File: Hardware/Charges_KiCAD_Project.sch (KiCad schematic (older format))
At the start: 33 parts, among them IC1 TP124005-2, J1 TB002-500-04BE, J2 TB002-500-04BE, Q1 SI7232DN-T1-GE3, Q2 SI7232DN-T1-GE3

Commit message: Changes to PCB size and components
PCB size was changed by adding 3mm to the top and bottom, the screw terminal was switched to a 90 degree angle one, and the libraries were updated
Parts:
- J1, J2: value TB002-500-04BE -> 796684-4; footprint SamacSys_Parts:TB00250004BE -> RDT_Custom_Footprints:TB00250004BE
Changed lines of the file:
@@
 P 7400 5500
 F 0 "J1" H 8028 5396 50  0000 L CNN
-F 1 "TB002-500-04BE" H 8028 5305 50  0000 L CNN
-F 2 "SamacSys_Parts:TB00250004BE" H 8050 5600 50  0001 L CNN
+F 1 "796684-4" H 8028 5305 50  0000 L CNN
+F 2 "RDT_Custom_Footprints:TB00250004BE" H 8050 5600 50  0001 L CNN
 F 3 "https://componentsearchengine.com/Datasheets/1/TB002-500-04BE.pdf" H 8050 5500 50  0001 L CNN
 F 4 "Fixed Terminal Blocks screw type, 5.00 , horizontal, 4 poles, CUI Blue, slotted screw, PCB mount" H 8050 5400 50  0001 L CNN "Description"
@@
 P 9850 5500
 F 0 "J2" H 10478 5396 50  0000 L CNN
-F 1 "TB002-500-04BE" H 10478 5305 50  0000 L CNN
-F 2 "SamacSys_Parts:TB00250004BE" H 10500 5600 50  0001 L CNN
+F 1 "796684-4" H 10478 5305 50  0000 L CNN
+F 2 "RDT_Custom_Footprints:TB00250004BE" H 10500 5600 50  0001 L CNN
 F 3 "https://componentsearchengine.com/Datasheets/1/TB002-500-04BE.pdf" H 10500 5500 50  0001 L CNN
 F 4 "Fixed Terminal Blocks screw type, 5.00 , horizontal, 4 poles, CUI Blue, slotted screw, PCB mount" H 10500 5400 50  0001 L CNN "Description"

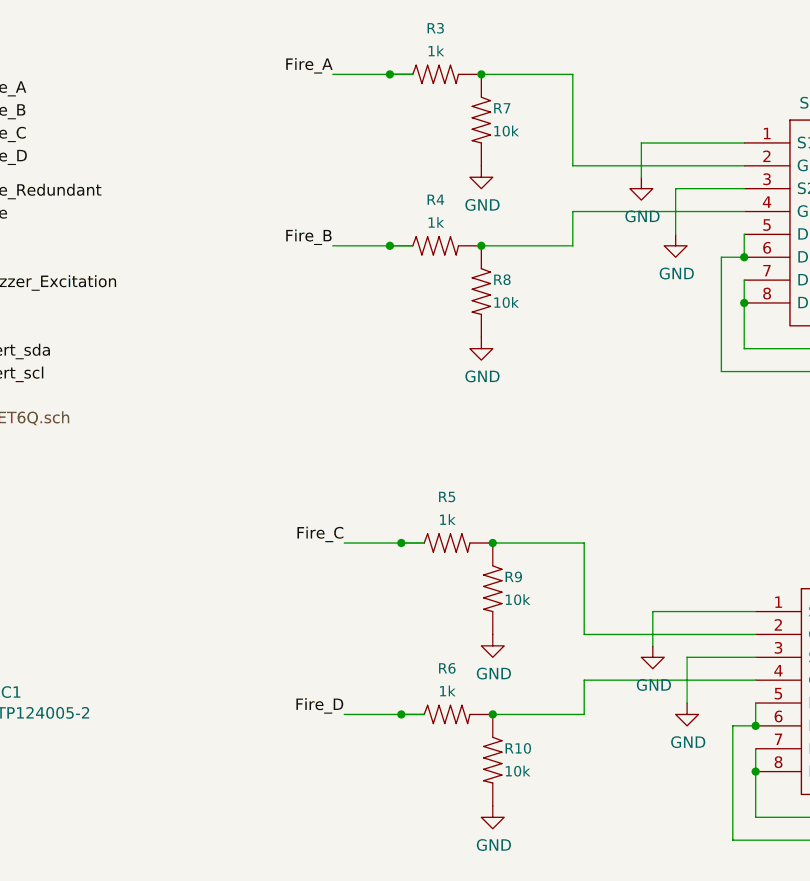
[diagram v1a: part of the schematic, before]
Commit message: Replaced passive component footprints with handsolder variants
Most components unaffected, redesign was needed around SI7232DN chips
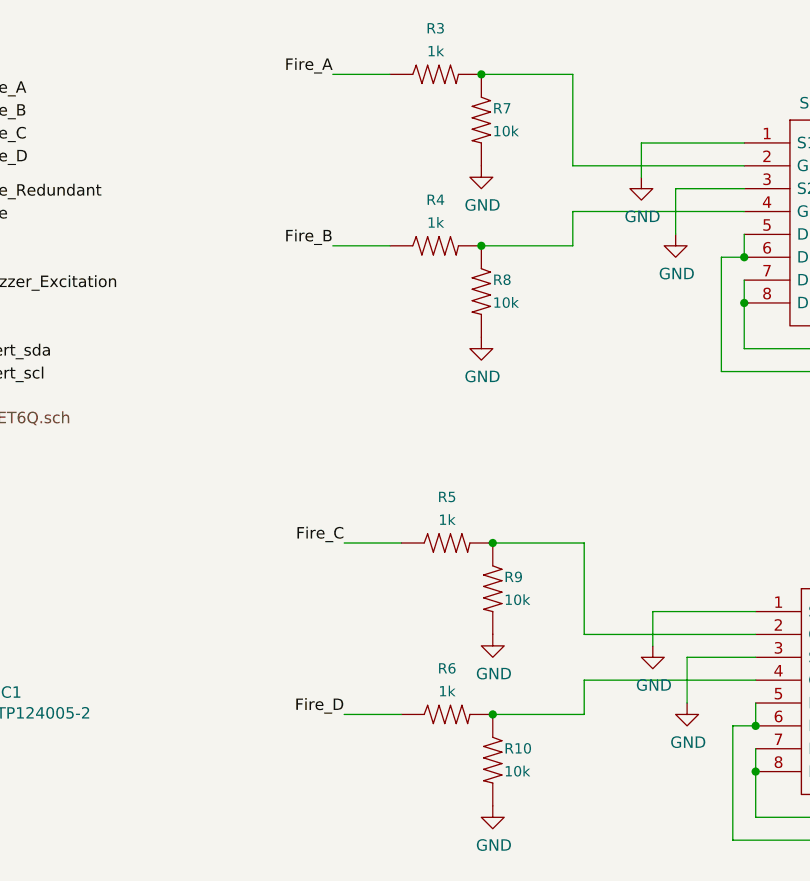
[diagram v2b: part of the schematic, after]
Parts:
- R1, R10, R11, R12, R13, R14, R15, R16, R17, R18, R19, R2, R20, R21, R22, R23, R24, R3, R4, R5, R6, R7, R8, R9: footprint Resistor_SMD:R_0603_1608Metric -> Resistor_SMD:R_0603_1608Metric_Pad1.05x0.95mm_HandSolder
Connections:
- wire segments 113 -> 109
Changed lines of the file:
@@
 Wire Wire Line
 	6650 3000 6400 3000
-Connection ~ 6650 3000
 Connection ~ 7050 3750
 Wire Wire Line
 	6650 3750 6400 3750
-Connection ~ 6650 3750
 $Comp
 L Charges_KiCAD_Project-rescue:RESISTOR0402-SparkFun-Resistors R9
@@
 F 0 "R9" V 7000 3250 45  0000 L CNN
 F 1 "10k" V 7100 3250 45  0000 L CNN
-F 2 "Resistor_SMD:R_0603_1608Metric" H 7050 3350 20  0001 C CNN
+F 2 "Resistor_SMD:R_0603_1608Metric_Pad1.05x0.95mm_HandSolder" H 7050 3350 20  0001 C CNN
 F 3 "" H 7050 3200 60  0001 C CNN
 F 4 " " V 7134 3268 60  0000 L CNN "Field4"
@@
 	1    0    0    -1
 $EndComp
-Wire Wire Line
-	6750 3000 6650 3000
 $Comp
 L power:GND #PWR010
@@
 F 0 "R10" V 7000 4000 45  0000 L CNN
 F 1 "10k" V 7100 4000 45  0000 L CNN
-F 2 "Resistor_SMD:R_0603_1608Metric" H 7050 4100 20  0001 C CNN
+F 2 "Resistor_SMD:R_0603_1608Metric_Pad1.05x0.95mm_HandSolder" H 7050 4100 20  0001 C CNN
 F 3 "" H 7050 3950 60  0001 C CNN
 F 4 " " V 7134 4018 60  0000 L CNN "Field4"
@@
 F 0 "R6" H 6850 3950 45  0000 C CNN
 F 1 "1k" H 6850 3850 45  0000 C CNN
-F 2 "Resistor_SMD:R_0603_1608Metric" H 6850 3900 20  0001 C CNN
+F 2 "Resistor_SMD:R_0603_1608Metric_Pad1.05x0.95mm_HandSolder" H 6850 3900 20  0001 C CNN
 F 3 "" H 6850 3750 60  0001 C CNN
 F 4 " " H 6850 3871 60  0000 C CNN "Field4"
@@
 	1    0    0    -1
 $EndComp
-Wire Wire Line
-	6750 3750 6650 3750
 Wire Wire Line
 	10450 3950 10700 3950
@@
 F 0 "R23" V 10400 3400 45  0000 L CNN
 F 1 "27k" V 10500 3400 45  0000 L CNN
-F 2 "Resistor_SMD:R_0603_1608Metric" H 10450 3450 20  0001 C CNN
+F 2 "Resistor_SMD:R_0603_1608Metric_Pad1.05x0.95mm_HandSolder" H 10450 3450 20  0001 C CNN
 F 3 "" H 10450 3300 60  0001 C CNN
 F 4 " " V 10534 3368 60  0000 L CNN "Field4"
@@
 F 0 "R19" H 10250 3250 45  0000 C CNN
 F 1 "100k" H 10250 3200 45  0000 C CNN
-F 2 "Resistor_SMD:R_0603_1608Metric" H 10250 3250 20  0001 C CNN
+F 2 "Resistor_SMD:R_0603_1608Metric_Pad1.05x0.95mm_HandSolder" H 10250 3250 20  0001 C CNN
 F 3 "" H 10250 3100 60  0001 C CNN
 F 4 " " H 10250 3221 60  0000 C CNN "Field4"
@@
 F 0 "R24" V 10400 4250 45  0000 L CNN
 F 1 "27k" V 10500 4250 45  0000 L CNN
-F 2 "Resistor_SMD:R_0603_1608Metric" H 10450 4300 20  0001 C CNN
+F 2 "Resistor_SMD:R_0603_1608Metric_Pad1.05x0.95mm_HandSolder" H 10450 4300 20  0001 C CNN
 F 3 "" H 10450 4150 60  0001 C CNN
 F 4 " " V 10534 4218 60  0000 L CNN "Field4"
@@
 F 0 "R20" H 10250 4100 45  0000 C CNN
 F 1 "100k" H 10250 4050 45  0000 C CNN
-F 2 "Resistor_SMD:R_0603_1608Metric" H 10250 4100 20  0001 C CNN
+F 2 "Resistor_SMD:R_0603_1608Metric_Pad1.05x0.95mm_HandSolder" H 10250 4100 20  0001 C CNN
 F 3 "" H 10250 3950 60  0001 C CNN
 F 4 " " H 10250 4071 60  0000 C CNN "Field4"
@@
 F 0 "R5" H 6850 3200 45  0000 C CNN
 F 1 "1k" H 6850 3100 45  0000 C CNN
-F 2 "Resistor_SMD:R_0603_1608Metric" H 6850 3150 20  0001 C CNN
+F 2 "Resistor_SMD:R_0603_1608Metric_Pad1.05x0.95mm_HandSolder" H 6850 3150 20  0001 C CNN
 F 3 "" H 6850 3000 60  0001 C CNN
 F 4 " " H 6850 3121 60  0000 C CNN "Field4"
@@
 Wire Wire Line
 	6600 950  6350 950
-Connection ~ 6600 950
 Connection ~ 7000 1700
 Wire Wire Line
 	6600 1700 6350 1700
-Connection ~ 6600 1700
 $Comp
 L Charges_KiCAD_Project-rescue:RESISTOR0402-SparkFun-Resistors R7
@@
 F 0 "R7" V 6950 1200 45  0000 L CNN
 F 1 "10k" V 7050 1200 45  0000 L CNN
-F 2 "Resistor_SMD:R_0603_1608Metric" H 7000 1300 20  0001 C CNN
+F 2 "Resistor_SMD:R_0603_1608Metric_Pad1.05x0.95mm_HandSolder" H 7000 1300 20  0001 C CNN
 F 3 "" H 7000 1150 60  0001 C CNN
 F 4 " " V 7084 1218 60  0000 L CNN "Field4"
@@
 	1    0    0    -1
 $EndComp
-Wire Wire Line
-	6700 950  6600 950
 $Comp
 L power:GND #PWR08
@@
 F 0 "R8" V 6950 1950 45  0000 L CNN
 F 1 "10k" V 7050 1950 45  0000 L CNN
-F 2 "Resistor_SMD:R_0603_1608Metric" H 7000 2050 20  0001 C CNN
+F 2 "Resistor_SMD:R_0603_1608Metric_Pad1.05x0.95mm_HandSolder" H 7000 2050 20  0001 C CNN
 F 3 "" H 7000 1900 60  0001 C CNN
 F 4 " " V 7084 1968 60  0000 L CNN "Field4"
@@
 F 0 "R15" H 9500 5650 45  0000 C CNN
 F 1 "0.25" H 9500 5600 45  0000 C CNN
-F 2 "Resistor_SMD:R_0603_1608Metric" H 9500 5650 20  0001 C CNN
+F 2 "Resistor_SMD:R_0603_1608Metric_Pad1.05x0.95mm_HandSolder" H 9500 5650 20  0001 C CNN
 F 3 "" H 9500 5500 60  0001 C CNN
 F 4 " " H 9500 5621 60  0000 C CNN "Field4"
@@
 F 0 "R13" H 9100 5400 45  0000 C CNN
 F 1 "10" H 9100 5350 45  0000 C CNN
-F 2 "Resistor_SMD:R_0603_1608Metric" H 9100 5650 20  0001 C CNN
+F 2 "Resistor_SMD:R_0603_1608Metric_Pad1.05x0.95mm_HandSolder" H 9100 5650 20  0001 C CNN
 F 3 "" H 9100 5500 60  0001 C CNN
 F 4 " " H 9100 5621 60  0000 C CNN "Field4"
@@
 F 0 "R14" H 9100 5700 45  0000 C CNN
 F 1 "10" H 9100 5650 45  0000 C CNN
-F 2 "Resistor_SMD:R_0603_1608Metric" H 9100 5950 20  0001 C CNN
+F 2 "Resistor_SMD:R_0603_1608Metric_Pad1.05x0.95mm_HandSolder" H 9100 5950 20  0001 C CNN
 F 3 "" H 9100 5800 60  0001 C CNN
 F 4 " " H 9100 5921 60  0000 C CNN "Field4"
@@
 F 0 "R16" H 9500 5950 45  0000 C CNN
 F 1 "0.25" H 9500 5900 45  0000 C CNN
-F 2 "Resistor_SMD:R_0603_1608Metric" H 9500 5950 20  0001 C CNN
+F 2 "Resistor_SMD:R_0603_1608Metric_Pad1.05x0.95mm_HandSolder" H 9500 5950 20  0001 C CNN
 F 3 "" H 9500 5800 60  0001 C CNN
 F 4 " " H 9500 5921 60  0000 C CNN "Field4"
@@
 F 0 "R4" H 6800 1900 45  0000 C CNN
 F 1 "1k" H 6800 1800 45  0000 C CNN
-F 2 "Resistor_SMD:R_0603_1608Metric" H 6800 1850 20  0001 C CNN
+F 2 "Resistor_SMD:R_0603_1608Metric_Pad1.05x0.95mm_HandSolder" H 6800 1850 20  0001 C CNN
 F 3 "" H 6800 1700 60  0001 C CNN
 F 4 " " H 6800 1821 60  0000 C CNN "Field4"
@@
 F 0 "R21" V 10350 1350 45  0000 L CNN
 F 1 "27k" V 10450 1350 45  0000 L CNN
-F 2 "Resistor_SMD:R_0603_1608Metric" H 10400 1400 20  0001 C CNN
+F 2 "Resistor_SMD:R_0603_1608Metric_Pad1.05x0.95mm_HandSolder" H 10400 1400 20  0001 C CNN
 F 3 "" H 10400 1250 60  0001 C CNN
 F 4 " " V 10484 1318 60  0000 L CNN "Field4"
@@
 F 0 "R17" H 10200 1200 45  0000 C CNN
 F 1 "100k" H 10200 1150 45  0000 C CNN
-F 2 "Resistor_SMD:R_0603_1608Metric" H 10200 1200 20  0001 C CNN
+F 2 "Resistor_SMD:R_0603_1608Metric_Pad1.05x0.95mm_HandSolder" H 10200 1200 20  0001 C CNN
 F 3 "" H 10200 1050 60  0001 C CNN
 F 4 " " H 10200 1171 60  0000 C CNN "Field4"
@@
 F 0 "R22" V 10350 2200 45  0000 L CNN
 F 1 "27k" V 10450 2200 45  0000 L CNN
-F 2 "Resistor_SMD:R_0603_1608Metric" H 10400 2250 20  0001 C CNN
+F 2 "Resistor_SMD:R_0603_1608Metric_Pad1.05x0.95mm_HandSolder" H 10400 2250 20  0001 C CNN
 F 3 "" H 10400 2100 60  0001 C CNN
 F 4 " " V 10484 2168 60  0000 L CNN "Field4"
@@
 F 0 "R3" H 6800 1150 45  0000 C CNN
 F 1 "1k" H 6800 1050 45  0000 C CNN
-F 2 "Resistor_SMD:R_0603_1608Metric" H 6800 1100 20  0001 C CNN
+F 2 "Resistor_SMD:R_0603_1608Metric_Pad1.05x0.95mm_HandSolder" H 6800 1100 20  0001 C CNN
 F 3 "" H 6800 950 60  0001 C CNN
 F 4 " " H 6800 1071 60  0000 C CNN "Field4"
@@
 F 0 "R18" H 10200 2050 45  0000 C CNN
 F 1 "100k" H 10200 2000 45  0000 C CNN
-F 2 "Resistor_SMD:R_0603_1608Metric" H 10200 2050 20  0001 C CNN
+F 2 "Resistor_SMD:R_0603_1608Metric_Pad1.05x0.95mm_HandSolder" H 10200 2050 20  0001 C CNN
 F 3 "" H 10200 1900 60  0001 C CNN
 F 4 " " H 10200 2021 60  0000 C CNN "Field4"
@@
 	1    0    0    -1
 $EndComp
-Wire Wire Line
-	6700 1700 6600 1700
 $Comp
 L Charges_KiCAD_Project-rescue:SI7232DN-T1-GE3-SamacSys_Parts Q1
@@
 F 0 "R2" H 6650 5700 45  0000 C CNN
 F 1 "10" H 6650 5650 45  0000 C CNN
-F 2 "Resistor_SMD:R_0603_1608Metric" H 6650 5950 20  0001 C CNN
+F 2 "Resistor_SMD:R_0603_1608Metric_Pad1.05x0.95mm_HandSolder" H 6650 5950 20  0001 C CNN
 F 3 "" H 6650 5800 60  0001 C CNN
 F 4 " " H 6650 5921 60  0000 C CNN "Field4"
@@
 F 0 "R1" H 6650 5400 45  0000 C CNN
 F 1 "10" H 6650 5350 45  0000 C CNN
-F 2 "Resistor_SMD:R_0603_1608Metric" H 6650 5650 20  0001 C CNN
+F 2 "Resistor_SMD:R_0603_1608Metric_Pad1.05x0.95mm_HandSolder" H 6650 5650 20  0001 C CNN
 F 3 "" H 6650 5500 60  0001 C CNN
 F 4 " " H 6650 5621 60  0000 C CNN "Field4"
@@
 F 0 "R12" H 7050 5950 45  0000 C CNN
 F 1 "0.25" H 7050 5900 45  0000 C CNN
-F 2 "Resistor_SMD:R_0603_1608Metric" H 7050 5950 20  0001 C CNN
+F 2 "Resistor_SMD:R_0603_1608Metric_Pad1.05x0.95mm_HandSolder" H 7050 5950 20  0001 C CNN
 F 3 "" H 7050 5800 60  0001 C CNN
 F 4 " " H 7050 5921 60  0000 C CNN "Field4"
@@
 F 0 "R11" H 7050 5650 45  0000 C CNN
 F 1 "0.25" H 7050 5600 45  0000 C CNN
-F 2 "Resistor_SMD:R_0603_1608Metric" H 7050 5650 20  0001 C CNN
+F 2 "Resistor_SMD:R_0603_1608Metric_Pad1.05x0.95mm_HandSolder" H 7050 5650 20  0001 C CNN
 F 3 "" H 7050 5500 60  0001 C CNN
 F 4 " " H 7050 5621 60  0000 C CNN "Field4"

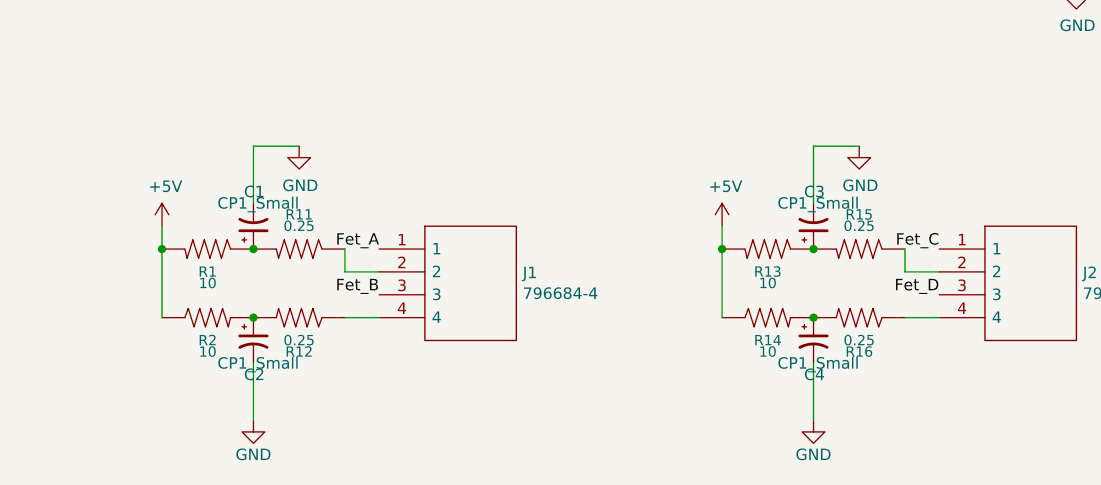
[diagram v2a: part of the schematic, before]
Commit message: update to caps and board layout
caps were changed and resistors were removed as they were not needed
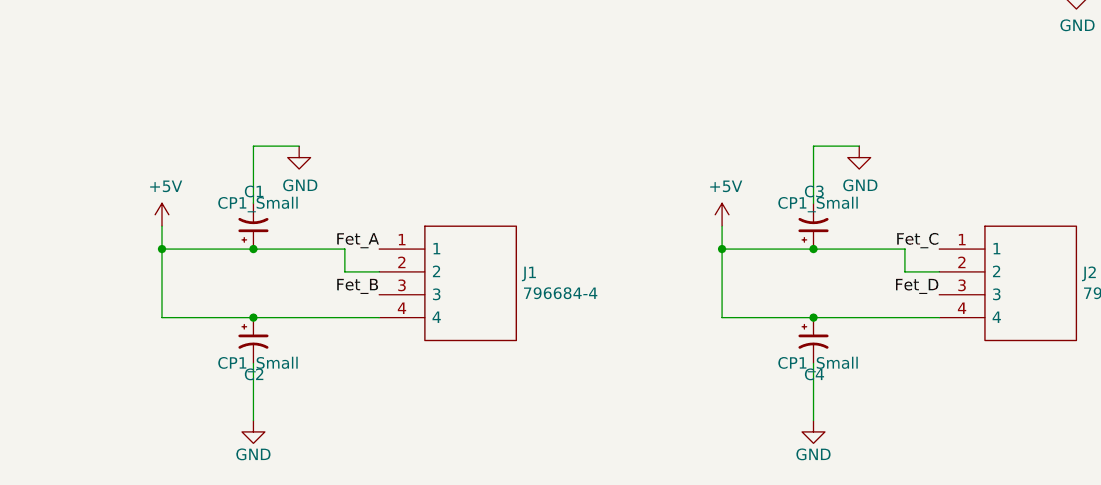
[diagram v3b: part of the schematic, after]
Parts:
- removed R1, R13, R14, R2: 10, Resistor_SMD:R_0603_1608Metric_Pad1.05x0.95mm_HandSolder, symbol Charges_KiCAD_Project-rescue:RESISTOR0402-SparkFun-Resistors
- removed R11, R12, R15, R16: 0.25, Resistor_SMD:R_0603_1608Metric_Pad1.05x0.95mm_HandSolder, symbol Charges_KiCAD_Project-rescue:RESISTOR0402-SparkFun-Resistors
- C1, C2, C3, C4: footprint Capacitor_THT:CP_Axial_L10.0mm_D4.5mm_P15.00mm_Horizontal -> Capacitor_THT:CP_Axial_L18.0mm_D6.5mm_P25.00mm_Horizontal
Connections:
- net +5V: now also C1.1, C2.1, C3.1, C4.1, J1.2, J1.4, J2.2, J2.4
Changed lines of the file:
@@
 	1    0    0    -1
 $EndComp
-Wire Wire Line
-	8900 5500 8900 5400
-Connection ~ 8900 5500
 $Comp
 L power:GND #PWR02
@@
 $EndComp
 Wire Wire Line
-	7400 5800 7250 5800
-Wire Wire Line
 	7250 5600 7400 5600
 Text Label 7400 5500 2    50   ~ 0
@@
 F 0 "C2" H 6900 5750 50  0000 R CNN
 F 1 "CP1_Small" H 7050 5800 50  0000 R CNN
-F 2 "Capacitor_THT:CP_Axial_L10.0mm_D4.5mm_P15.00mm_Horizontal" H 6850 5900 50  0001 C CNN
+F 2 "Capacitor_THT:CP_Axial_L18.0mm_D6.5mm_P25.00mm_Horizontal" H 6850 5900 50  0001 C CNN
 F 3 "~" H 6850 5900 50  0001 C CNN
 	1    6850 5900
 	1    0    0    -1
 $EndComp
-Connection ~ 6850 5800
 Wire Wire Line
 	6850 6000 6850 6250
@@
 	1    0    0    -1
 $EndComp
-Connection ~ 6850 5500
 $Comp
 L Device:CP1_Small C1
@@
 F 0 "C1" H 6900 5250 50  0000 R CNN
 F 1 "CP1_Small" H 7050 5300 50  0000 R CNN
-F 2 "Capacitor_THT:CP_Axial_L10.0mm_D4.5mm_P15.00mm_Horizontal" H 6850 5400 50  0001 C CNN
+F 2 "Capacitor_THT:CP_Axial_L18.0mm_D6.5mm_P25.00mm_Horizontal" H 6850 5400 50  0001 C CNN
 F 3 "~" H 6850 5400 50  0001 C CNN
 	1    6850 5400
@@
 Wire Wire Line
 	7250 5600 7250 5500
-Wire Wire Line
-	6450 5800 6450 5500
-Wire Wire Line
-	6450 5500 6450 5400
-Connection ~ 6450 5500
 $Comp
 L power:+5V #PWR05
@@
 Wire Wire Line
 	1050 3800 1150 3800
-Wire Wire Line
-	8900 5800 8900 5500
 Text Label 2350 2150 0    50   ~ 0
 Fire_Redundant
@@
 F 0 "C3" H 9350 5250 50  0000 R CNN
 F 1 "CP1_Small" H 9500 5300 50  0000 R CNN
-F 2 "Capacitor_THT:CP_Axial_L10.0mm_D4.5mm_P15.00mm_Horizontal" H 9300 5400 50  0001 C CNN
+F 2 "Capacitor_THT:CP_Axial_L18.0mm_D6.5mm_P25.00mm_Horizontal" H 9300 5400 50  0001 C CNN
 F 3 "~" H 9300 5400 50  0001 C CNN
 	1    9300 5400
 	1    0    0    1
 $EndComp
-$Comp
-L Charges_KiCAD_Project-rescue:RESISTOR0402-SparkFun-Resistors R15
-U 1 1 61951EFA
-P 9500 5500
-F 0 "R15" H 9500 5650 45  0000 C CNN
-F 1 "0.25" H 9500 5600 45  0000 C CNN
-F 2 "Resistor_SMD:R_0603_1608Metric_Pad1.05x0.95mm_HandSolder" H 9500 5650 20  0001 C CNN
-F 3 "" H 9500 5500 60  0001 C CNN
-F 4 " " H 9500 5621 60  0000 C CNN "Field4"
-	1    9500 5500
-	-1   0    0    -1
-$EndComp
-$Comp
-L Charges_KiCAD_Project-rescue:RESISTOR0402-SparkFun-Resistors R13
-U 1 1 61951EF3
-P 9100 5500
-F 0 "R13" H 9100 5400 45  0000 C CNN
-F 1 "10" H 9100 5350 45  0000 C CNN
-F 2 "Resistor_SMD:R_0603_1608Metric_Pad1.05x0.95mm_HandSolder" H 9100 5650 20  0001 C CNN
-F 3 "" H 9100 5500 60  0001 C CNN
-F 4 " " H 9100 5621 60  0000 C CNN "Field4"
-	1    9100 5500
-	-1   0    0    -1
-$EndComp
-Connection ~ 9300 5500
 $Comp
 L power:GND #PWR018
@@
 Wire Wire Line
 	9300 6000 9300 6250
-Connection ~ 9300 5800
-$Comp
-L Charges_KiCAD_Project-rescue:RESISTOR0402-SparkFun-Resistors R14
-U 1 1 61951EDB
-P 9100 5800
-F 0 "R14" H 9100 5700 45  0000 C CNN
-F 1 "10" H 9100 5650 45  0000 C CNN
-F 2 "Resistor_SMD:R_0603_1608Metric_Pad1.05x0.95mm_HandSolder" H 9100 5950 20  0001 C CNN
-F 3 "" H 9100 5800 60  0001 C CNN
-F 4 " " H 9100 5921 60  0000 C CNN "Field4"
-	1    9100 5800
-	1    0    0    -1
-$EndComp
-$Comp
-L Charges_KiCAD_Project-rescue:RESISTOR0402-SparkFun-Resistors R16
-U 1 1 61951ED4
-P 9500 5800
-F 0 "R16" H 9500 5950 45  0000 C CNN
-F 1 "0.25" H 9500 5900 45  0000 C CNN
-F 2 "Resistor_SMD:R_0603_1608Metric_Pad1.05x0.95mm_HandSolder" H 9500 5950 20  0001 C CNN
-F 3 "" H 9500 5800 60  0001 C CNN
-F 4 " " H 9500 5921 60  0000 C CNN "Field4"
-	1    9500 5800
-	-1   0    0    1
-$EndComp
 $Comp
 L Device:CP1_Small C4
@@
 F 0 "C4" H 9350 5750 50  0000 R CNN
 F 1 "CP1_Small" H 9500 5800 50  0000 R CNN
-F 2 "Capacitor_THT:CP_Axial_L10.0mm_D4.5mm_P15.00mm_Horizontal" H 9300 5900 50  0001 C CNN
+F 2 "Capacitor_THT:CP_Axial_L18.0mm_D6.5mm_P25.00mm_Horizontal" H 9300 5900 50  0001 C CNN
 F 3 "~" H 9300 5900 50  0001 C CNN
 	1    9300 5900
@@
 Wire Wire Line
 	9700 5600 9850 5600
-Wire Wire Line
-	9850 5800 9700 5800
 Text Label 10600 850  0    50   ~ 0
 Fet_A
@@
 	1    8150 1250
 	1    0    0    -1
-$EndComp
-$Comp
-L Charges_KiCAD_Project-rescue:RESISTOR0402-SparkFun-Resistors R2
-U 1 1 61863444
-P 6650 5800
-F 0 "R2" H 6650 5700 45  0000 C CNN
-F 1 "10" H 6650 5650 45  0000 C CNN
-F 2 "Resistor_SMD:R_0603_1608Metric_Pad1.05x0.95mm_HandSolder" H 6650 5950 20  0001 C CNN
-F 3 "" H 6650 5800 60  0001 C CNN
-F 4 " " H 6650 5921 60  0000 C CNN "Field4"
-	1    6650 5800
-	1    0    0    -1
-$EndComp
-$Comp
-L Charges_KiCAD_Project-rescue:RESISTOR0402-SparkFun-Resistors R1
-U 1 1 61864F70
-P 6650 5500
-F 0 "R1" H 6650 5400 45  0000 C CNN
-F 1 "10" H 6650 5350 45  0000 C CNN
-F 2 "Resistor_SMD:R_0603_1608Metric_Pad1.05x0.95mm_HandSolder" H 6650 5650 20  0001 C CNN
-F 3 "" H 6650 5500 60  0001 C CNN
-F 4 " " H 6650 5621 60  0000 C CNN "Field4"
-	1    6650 5500
-	-1   0    0    -1
-$EndComp
-$Comp
-L Charges_KiCAD_Project-rescue:RESISTOR0402-SparkFun-Resistors R12
-U 1 1 61862CA7
-P 7050 5800
-F 0 "R12" H 7050 5950 45  0000 C CNN
-F 1 "0.25" H 7050 5900 45  0000 C CNN
-F 2 "Resistor_SMD:R_0603_1608Metric_Pad1.05x0.95mm_HandSolder" H 7050 5950 20  0001 C CNN
-F 3 "" H 7050 5800 60  0001 C CNN
-F 4 " " H 7050 5921 60  0000 C CNN "Field4"
-	1    7050 5800
-	-1   0    0    1
-$EndComp
-$Comp
-L Charges_KiCAD_Project-rescue:RESISTOR0402-SparkFun-Resistors R11
-U 1 1 61863D89
-P 7050 5500
-F 0 "R11" H 7050 5650 45  0000 C CNN
-F 1 "0.25" H 7050 5600 45  0000 C CNN
-F 2 "Resistor_SMD:R_0603_1608Metric_Pad1.05x0.95mm_HandSolder" H 7050 5650 20  0001 C CNN
-F 3 "" H 7050 5500 60  0001 C CNN
-F 4 " " H 7050 5621 60  0000 C CNN "Field4"
-	1    7050 5500
-	-1   0    0    -1
 $EndComp
 $Sheet
@@
 F12 "Fire_redundant" I R 2350 2150 50
 $EndSheet
+Wire Wire Line
+	6450 5400 6450 5500
+Wire Wire Line
+	6450 5800 6850 5800
+Wire Wire Line
+	6850 5800 7400 5800
+Connection ~ 6850 5800
+Wire Wire Line
+	6450 5500 6850 5500
+Connection ~ 6450 5500
+Wire Wire Line
+	6450 5500 6450 5800
+Wire Wire Line
+	6850 5500 7250 5500
+Connection ~ 6850 5500
+Wire Wire Line
+	8900 5400 8900 5500
+Wire Wire Line
+	9300 5500 8900 5500
+Connection ~ 8900 5500
+Wire Wire Line
+	8900 5500 8900 5800
+Wire Wire Line
+	9300 5500 9700 5500
+Connection ~ 9300 5500
+Wire Wire Line
+	9300 5800 9850 5800
+Wire Wire Line
+	9300 5800 8900 5800
+Connection ~ 9300 5800
 $EndSCHEMATC
